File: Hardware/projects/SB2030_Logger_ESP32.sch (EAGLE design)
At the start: 34 parts, among them SW1 CKTACTSWITCH, U1 ESP-WROOM-32, U2 MCP2562, U3 NCP1117ST50T3G, U4 NCP1117ST33T3G, U5 SN65C1168PWR, X1 1751280

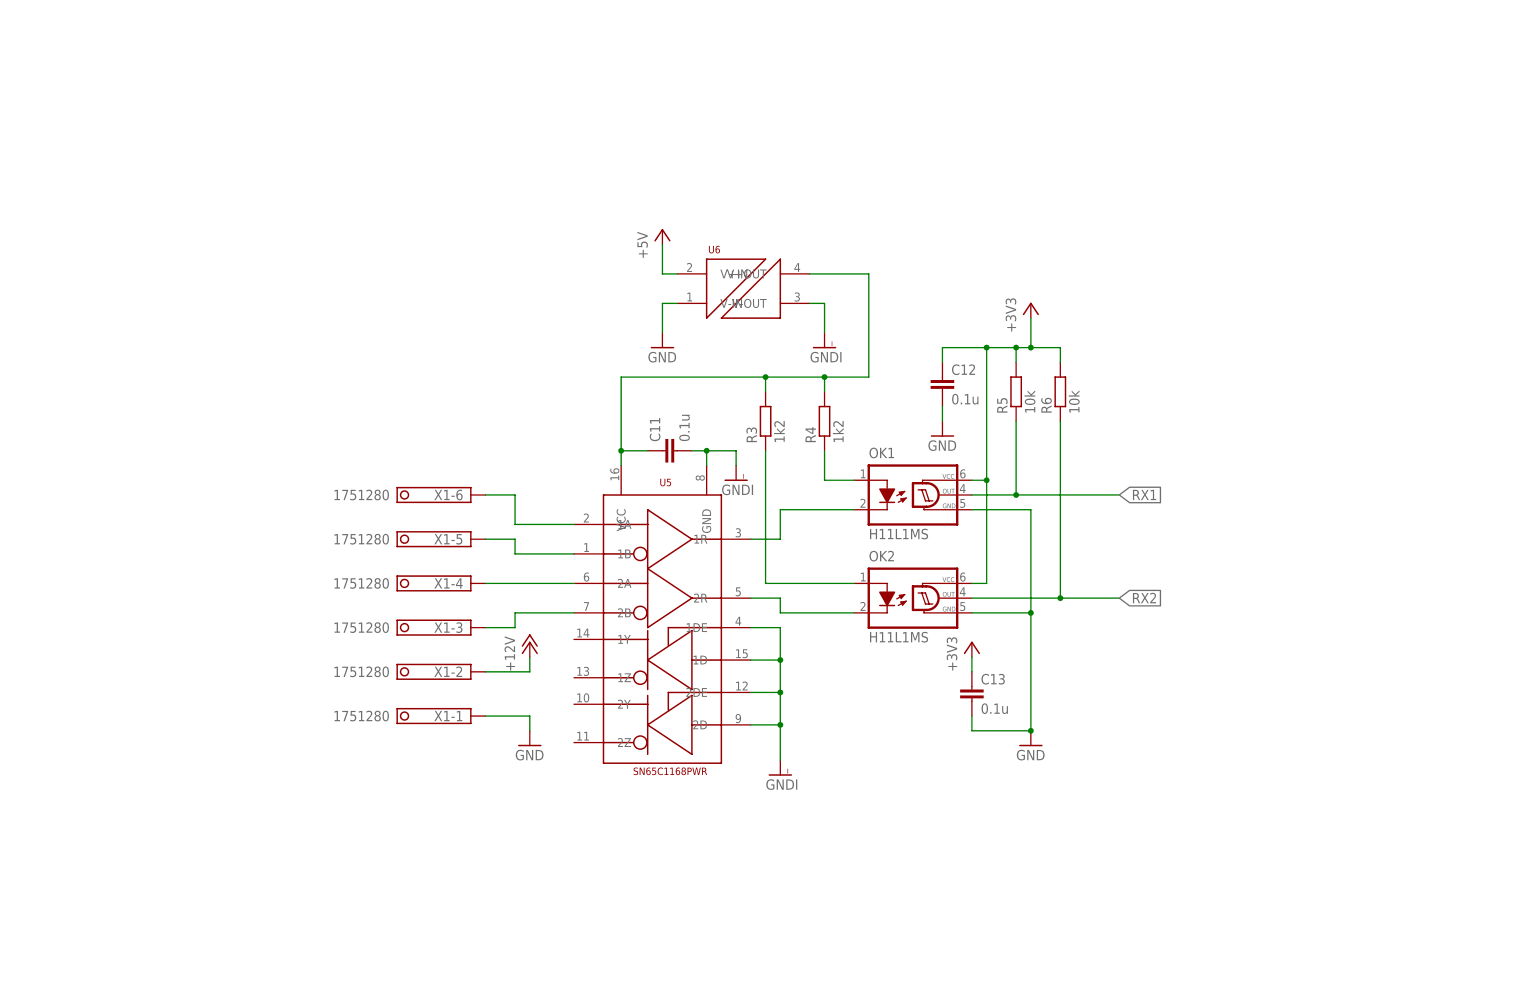
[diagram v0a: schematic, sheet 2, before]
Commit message: Major updates to SMD board design (added motion sensor and power management), with re-layout for production. Added Gerbers, BOM, and CPL for JLCPCB production. Added library for MPU6050 IMU. Added CCOM logo for silkscreen.
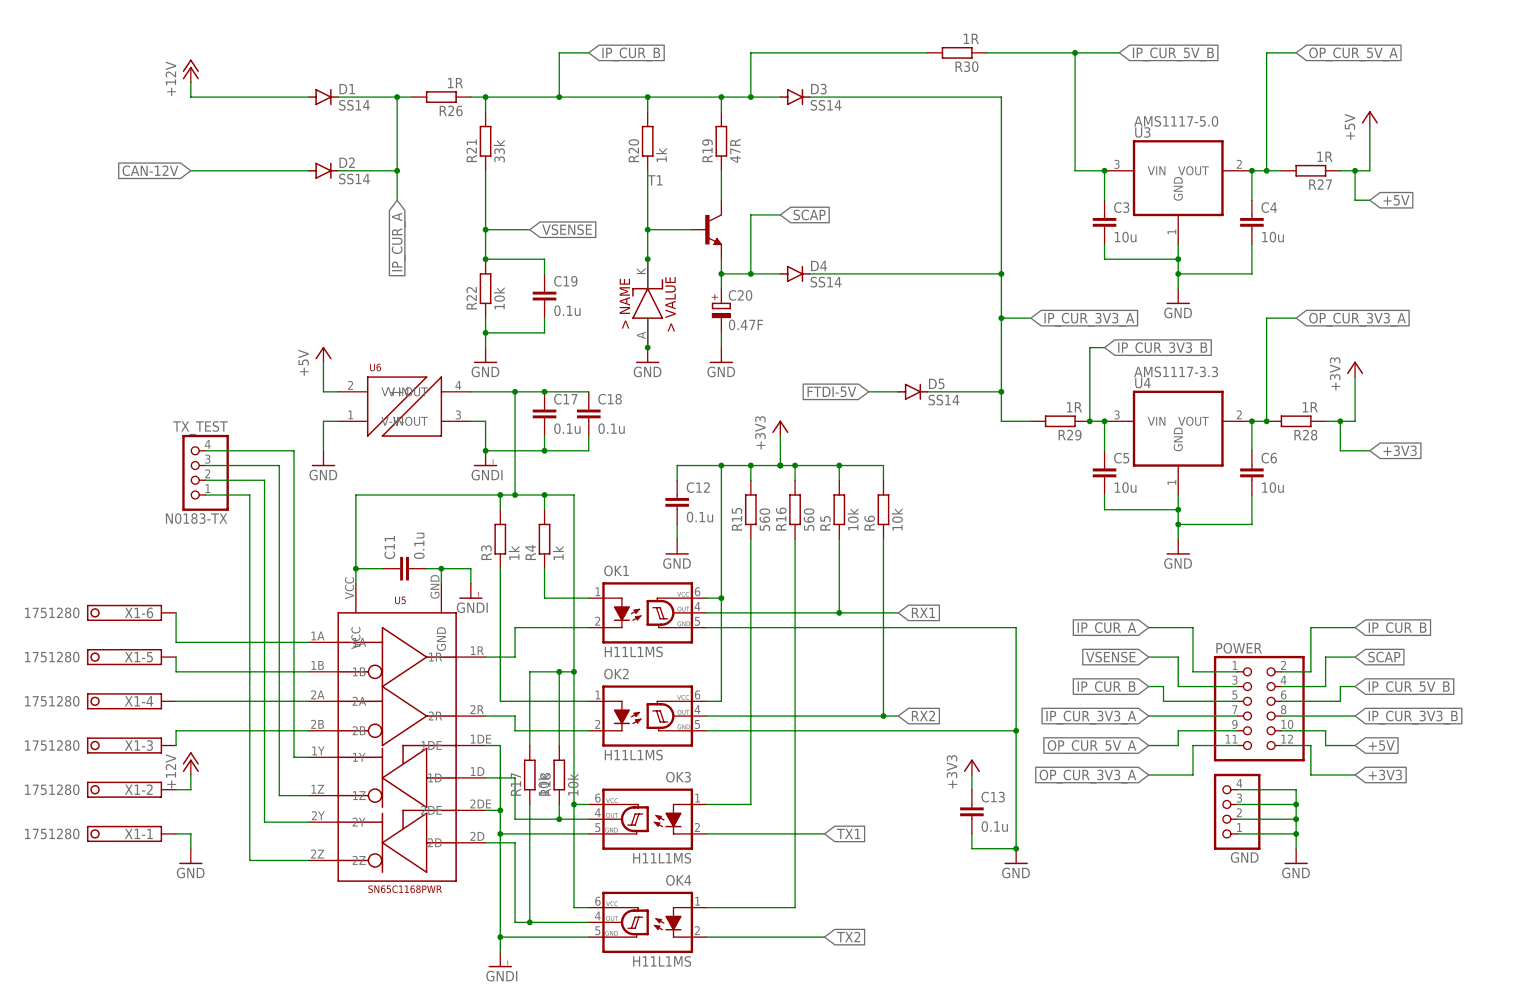
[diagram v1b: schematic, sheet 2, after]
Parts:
- removed JP1: FTDI/ICSP, pinhead:PINHD-1X6
- removed SDCARD: MicroSD Holder, 1140084168:1140084168
- removed SW1: CKTACTSWITCH, sb2030_logger:CKTACTSWITCH
- added C14: 2n2, rcl:C-EUC0805
- added C15, C17, C18, C19: 0.1u, rcl:C-EUC0805
- added C16: 10n, rcl:C-EUC0805
- added C20: 0.47F, rcl:CPOL-EUP128-50
- added CAN: CAN-TEST, pinhead:PINHD-1X2
- added D3, D4, D5: SS14, diode:CGRM4001-G
- added DZL4734: (no value), sb2030_logger:DZL4734
- added FTDI: FTDI/ICSP, pinhead:PINHD-1X6
- added GND: (no value), pinhead:PINHD-1X4
- added I2C: I2C_TEST, pinhead:PINHD-1X2
- added IC1: MPU6050, invensense:MPU6050
- added LED1, LED2, LED3: (no value), led:LEDCHIP-LED0603
- added N0183-TX: TX_TEST, pinhead:PINHD-1X4
- added NMEA2000: NMEA2000-2, pinhead:PINHD-1X4
- added OK3, OK4: H11L1MS, optocoupler:H11L1MS
- added POWER: (no value), pinhead:PINHD-2X6
- added PROG: PROG, pinhead:PINHD-1X2
- added R10, R11, R12, R13, R14, R9: 47k, rcl:R-EU_R0805
- added R15, R16: 560, rcl:R-EU_R0805
- added R17, R18, R22, R7, R8: 10k, rcl:R-EU_R0805
- added R19: 47R, rcl:R-EU_R0805
- added R20: 1k, rcl:R-EU_R0805
- added R21: 33k, rcl:R-EU_R0805
- added R23, R24, R25: 220, rcl:R-EU_R0805
- added R26, R27, R28, R29, R30: 1R, rcl:R-EU_R0805
- added R31: 6k8, rcl:R-EU_R0805
- added RESET: RESET, pinhead:PINHD-1X2
- added SDIO: SDIO_TEST, pinhead:PINHD-1X6
- added SJ1, SJ2, SJ3: (no value), jumper:SJ
- added T1: (no value), transistor:BC817-16-NPN-SOT23-BEC
- added T2, T3, T4: S8050, transistor:BC846
- added U$1: MICRO-SD, sb2030_logger:XUNPU-MICROSD-SOCKET
- D1, D2: value 1N5819 -> SS14; device sb2030_logger:1N5819HW-7-F -> diode:CGRM4001-G
- R3, R4: value 1k2 -> 1k
- U3: value NCP1117ST50T3G -> AMS1117-5.0
- U4: value NCP1117ST33T3G -> AMS1117-3.3
- U5: device sb2030_logger:SN65C1168PWR -> sb2030_logger:SN65C1168-SOIC
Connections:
- removed net VIN: C3.1, C5.1, D1.2, D2.2, U3.VIN, U4.VIN
- new net CAN-12V: D2.A, JP2.12V, NMEA2000.1
- new net FTDI-5V: D5.A, FTDI.3
- new net IP_CUR_3V3_A: D3.C, D4.C, D5.C, POWER.7, R29.2
- new net IP_CUR_3V3_B: C5.1, POWER.8, R29.1, U4.VIN
- new net IP_CUR_5V_B: C3.1, POWER.6, R30.1, U3.VIN
- new net IP_CUR_A: D1.C, D2.C, POWER.1, R26.2
- new net IP_CUR_B: D3.A, POWER.2, POWER.5, R19.2, R20.2, R21.2, R26.1, R30.2
- new net N$11: R10.1, SDIO.2, U$1.DAT1, U1.IO4
- new net N$23: C14.1, IC1G$1.CPOUT
- new net N$24: R12.1, SDIO.4, U$1.DAT3, U1.IO13
- new net N$25: R13.1, SDIO.5, U$1.CLK, U1.IO14
- new net N$26: R14.1, SDIO.6, U$1.CMD, U1.IO15
- new net N$27: N0183-TX.4, U5.1Y
- new net N$28: N0183-TX.3, U5.1Z
- new net N$29: N0183-TX.2, U5.2Y
- new net N$3: R1.1, SJ1.2
- new net N$30: N0183-TX.1, U5.2Z
- new net N$31: OK3.A, R15.1
- new net N$32: OK4.A, R16.1
- new net N$33: OK3.OUT, R18.1, U5.1D
- new net N$34: OK4.OUT, R17.1, U5.2D
- new net N$35: LED1.C, U1.IO25
- new net N$36: LED2.C, U1.IO26
- new net N$37: PROG.2, T2.B, T3.B, T4.B
- new net N$38: LED3.C, U1.IO27
- new net N$39: LED1.A, R23.2
- new net N$40: LED2.A, R24.2
- new net N$41: DZL4734.K, R20.1, T1.B
- new net N$42: R19.1, T1.C
- new net N$43: PROG.1, R31.1
- new net N$44: LED3.A, R25.2
- new net OP_CUR_3V3_A: C6.1, POWER.11, R28.2, U4.VOUT
- new net OP_CUR_5V_A: C4.1, POWER.9, R27.2, U3.VOUT
- new net SCAP: C20.+, D4.A, POWER.4, T1.E
- new net TX1: OK3.C, U1.IO18
- new net TX2: OK4.C, U1.IO19
- new net VSENSE: C19.1, POWER.3, R21.1, R22.2, U1.SENSOR_VP
- net +12V: now also D1.A; no longer D1.1
- net +3V3: now also C16.1, IC1G$1.VDD, IC1G$1.VLOGIC, POWER.12, R10.2, R11.2, R12.2, R13.2, R14.2, R15.2, R16.2, R23.1, R24.1, R25.1, R28.1, R31.2, R7.2, R8.2, R9.2, U$1.VCC; no longer C6.1, SDCARD.4, U4.VOUT
- net +5V: now also POWER.10, R27.1; no longer C4.1, U3.VOUT
- net GND: now also C14.2, C15.2, C16.2, C19.2, C20.-, DZL4734.A, FTDI.1, GND.1, GND.2, GND.3, GND.4, IC1G$1.AD0, IC1G$1.CLKIN, IC1G$1.FSYNC, IC1G$1.GND, IC1G$1.GND@1, NMEA2000.4, R22.1, RESET.2, T2.E, T3.E, T4.E, U$1.GND, U$1.GND1, U$1.GND2, U$1.GND3, U$1.GND4; no longer JP1.1, SDCARD.6, SW1.3, SW1.4
- net GNDI: now also C17.2, C18.2, OK3.GND, OK4.GND; no longer U5.1D, U5.2D
- net N$1: now also NMEA2000.2, R1.2; no longer R1.1
- net N$10: now also R11.1, SDIO.3, SJ3.1, SJ3.2, T4.C, U$1.DAT2, U1.IO12; no longer SDCARD.7, U1.IO19
- net N$12: now also T2.C; no longer SW1.1, SW1.2
- net N$2: now also NMEA2000.3, SJ1.1; no longer R1.2
- net N$21: now also C17.1, C18.1, OK3.VCC, OK4.VCC, R17.2, R18.2
- net N$22: now also R9.1, SDIO.1, SJ2.1, SJ2.2, T3.C, U$1.DAT0, U1.IO2; no longer D2.1, JP2.12V
- net N$4: now also RESET.1
- net N$5: now also I2C.2, IC1G$1.SCL, R7.1, U1.IO22; no longer SDCARD.2, U1.IO5
- net N$6: now also CAN.2
- net N$7: now also CAN.1, U1.IO17; no longer U1.IO4
- net N$8: now also I2C.1, IC1G$1.SDA, R8.1, U1.IO21; no longer SDCARD.3, U1.IO23
- net N$9: now also C15.1, IC1G$1.REGOUT; no longer SDCARD.5, U1.IO18
- net RX1: now also U1.IO34; no longer U1.IO13
- net RX2: now also U1.IO35; no longer U1.IO14
- net RXDATA: now also FTDI.5; no longer JP1.5
- net TXDATA: now also FTDI.4; no longer JP1.4
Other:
- moved on the sheet: C10, C11, C12, C13, C7, C8, C9, OK1, OK2, R1, R2, R3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

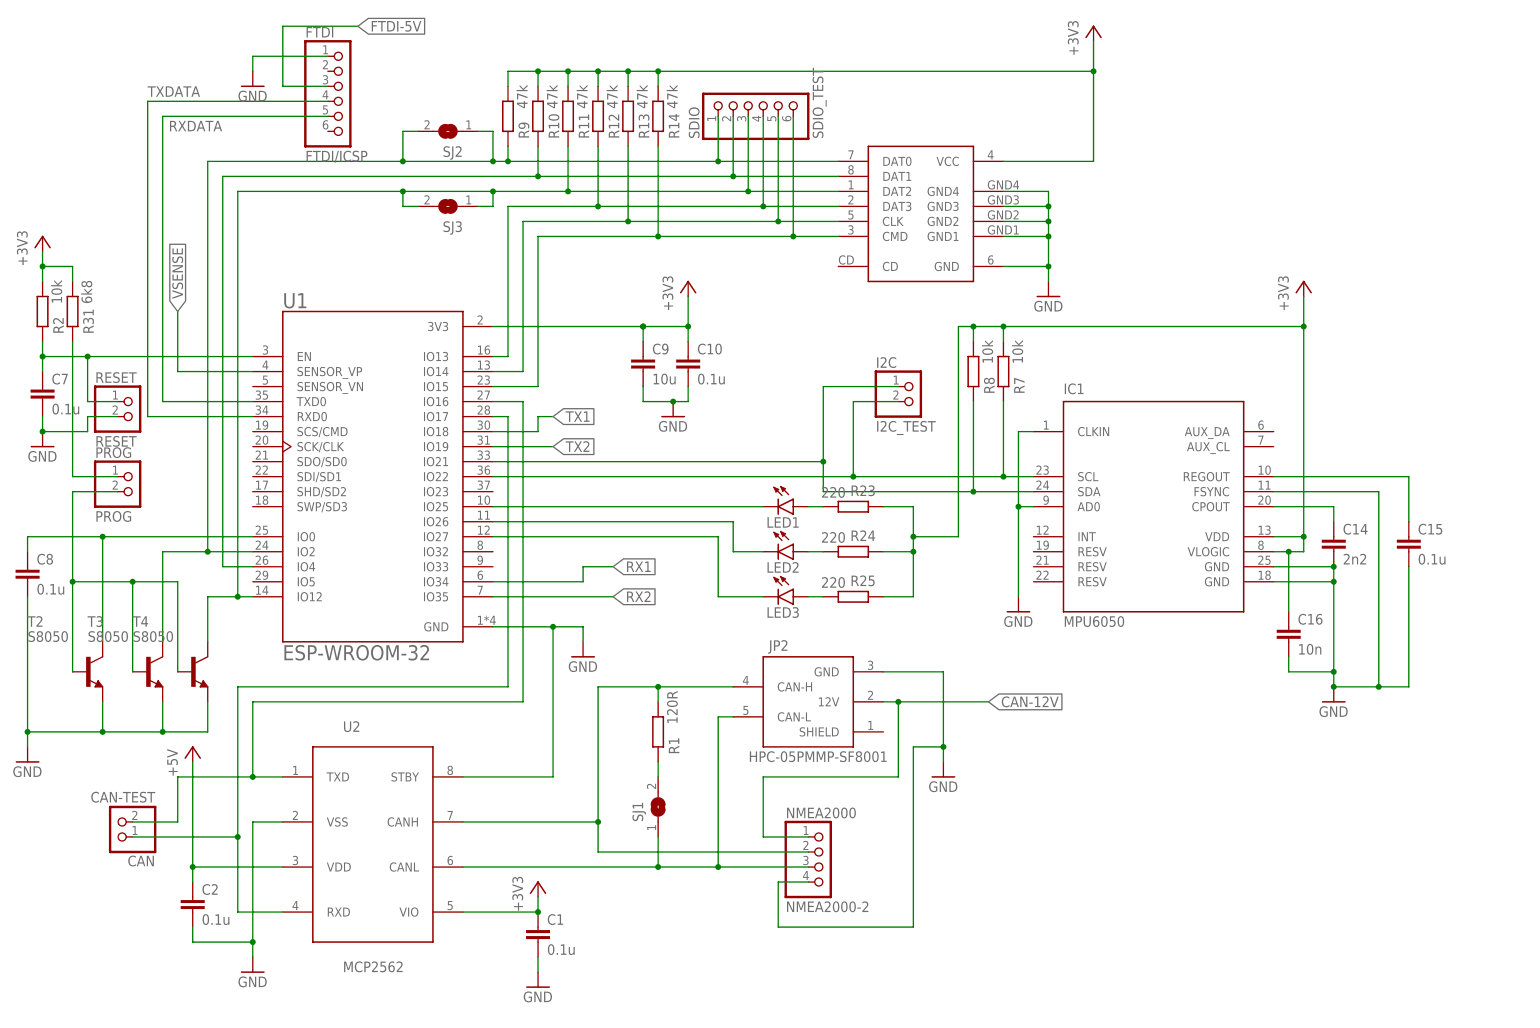
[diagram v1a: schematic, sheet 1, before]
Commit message: Updates to library specifications for devices, and schematic/board to match in order to give better match to actual components; V2.3 of demonstration board.
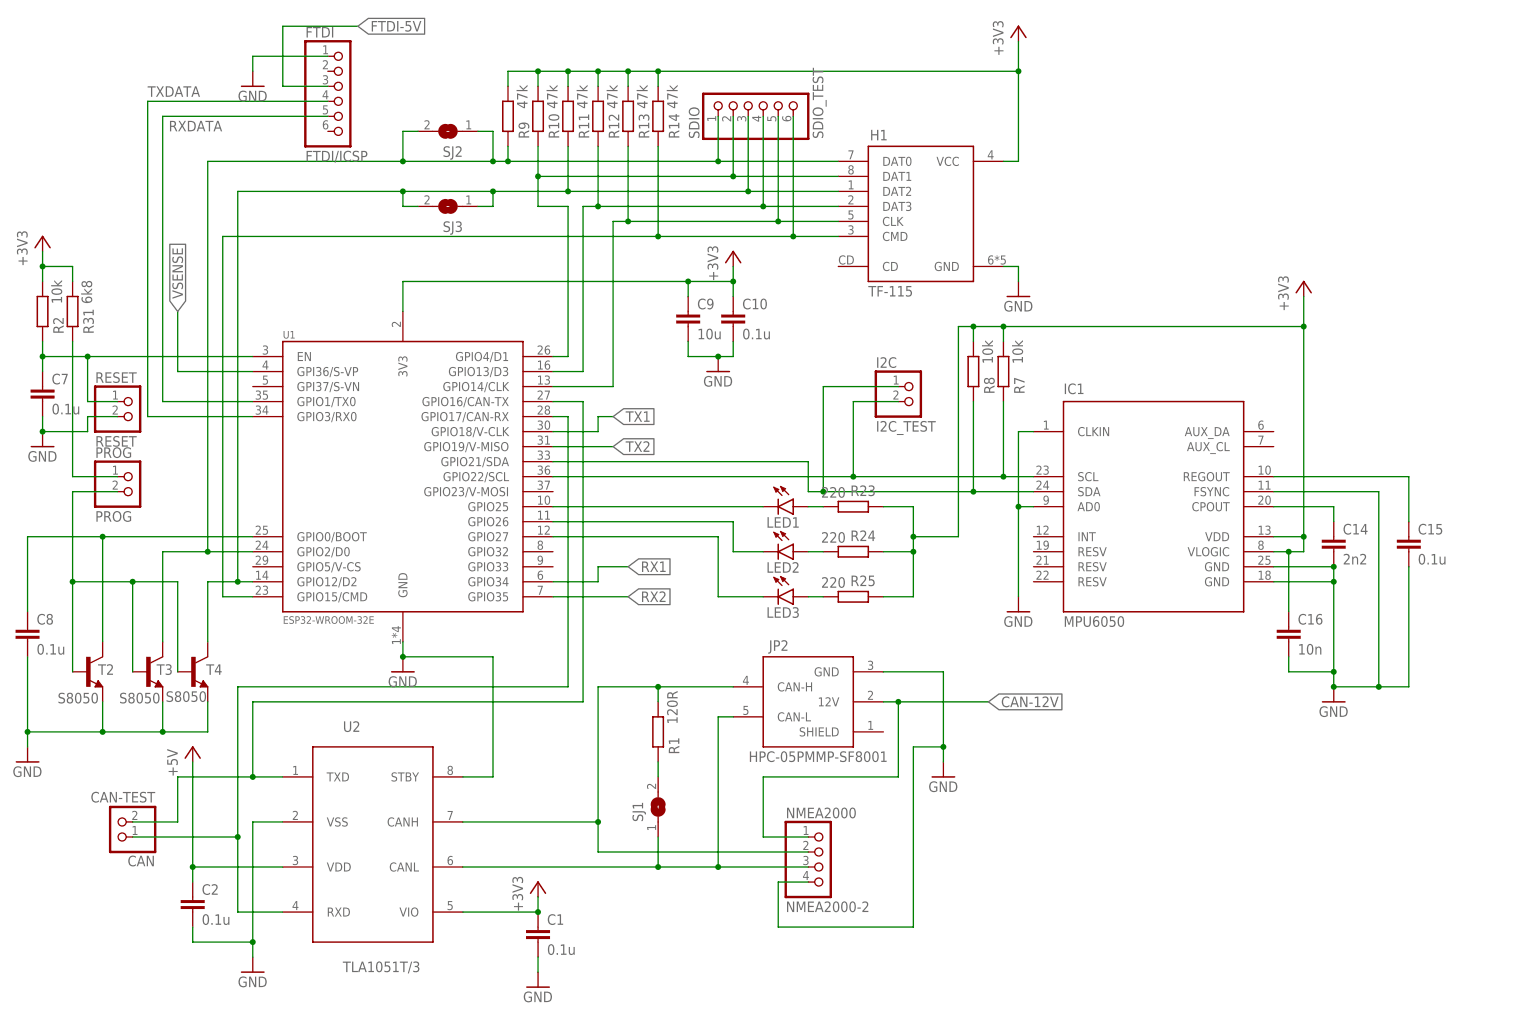
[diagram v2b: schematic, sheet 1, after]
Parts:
- removed DZL4734: (no value), sb2030_logger:DZL4734
- removed U$1: MICRO-SD, sb2030_logger:XUNPU-MICROSD-SOCKET
- added H1: TF-115, sb2030_logger:XUNPU-MICROSD-SOCKET
- added Z1: DZL4734, sb2030_logger:DZL4734
- D1, D2, D3, D4, D5: device diode:CGRM4001-G -> sb2030_logger:SS14
- U1: value ESP-WROOM-32 -> ESP32-WROOM-32E; device ESP-WROOM-32:ESP-WROOM-32 -> sb2030_logger:ESP32-WROOM-32E
- U2: value MCP2562 -> TLA1051T/3
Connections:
- net +3V3: now also H1.VCC; no longer U$1.VCC
- net GND: now also H1.GND, Z1.A; no longer DZL4734.A, U$1.GND, U$1.GND1, U$1.GND2, U$1.GND3, U$1.GND4
- net IP_CUR_3V3_A: now also D3.K, D4.K, D5.K; no longer D3.C, D4.C, D5.C
- net IP_CUR_A: now also D1.K, D2.K; no longer D1.C, D2.C
- net N$10: now also H1.DAT2, U1.GPIO12/D2; no longer U$1.DAT2, U1.IO12
- net N$11: now also H1.DAT1, U1.GPIO4/D1; no longer U$1.DAT1, U1.IO4
- net N$12: now also U1.GPIO0/BOOT; no longer U1.IO0
- net N$22: now also H1.DAT0, U1.GPIO2/D0; no longer U$1.DAT0, U1.IO2
- net N$24: now also H1.DAT3, U1.GPIO13/D3; no longer U$1.DAT3, U1.IO13
- net N$25: now also H1.CLK, U1.GPIO14/CLK; no longer U$1.CLK, U1.IO14
- net N$26: now also H1.CMD, U1.GPIO15/CMD; no longer U$1.CMD, U1.IO15
- net N$35: now also U1.GPIO25; no longer U1.IO25
- net N$36: now also U1.GPIO26; no longer U1.IO26
- net N$38: now also U1.GPIO27; no longer U1.IO27
- net N$41: now also Z1.K; no longer DZL4734.K
- net N$5: now also U1.GPIO22/SCL; no longer U1.IO22
- net N$6: now also U1.GPIO16/CAN-TX; no longer U1.IO16
- net N$7: now also U1.GPIO17/CAN-RX; no longer U1.IO17
- net N$8: now also U1.GPIO21/SDA; no longer U1.IO21
- net RX1: now also U1.GPIO34; no longer U1.IO34
- net RX2: now also U1.GPIO35; no longer U1.IO35
- net RXDATA: now also U1.GPIO1/TX0; no longer U1.TXD0
- net TX1: now also U1.GPIO18/V-CLK; no longer U1.IO18
- net TX2: now also U1.GPIO19/V-MISO; no longer U1.IO19
- net TXDATA: now also U1.GPIO3/RX0; no longer U1.RXD0
- net VSENSE: now also U1.GPI36/S-VP; no longer U1.SENSOR_VP
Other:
- moved on the sheet: C10, C8, C9

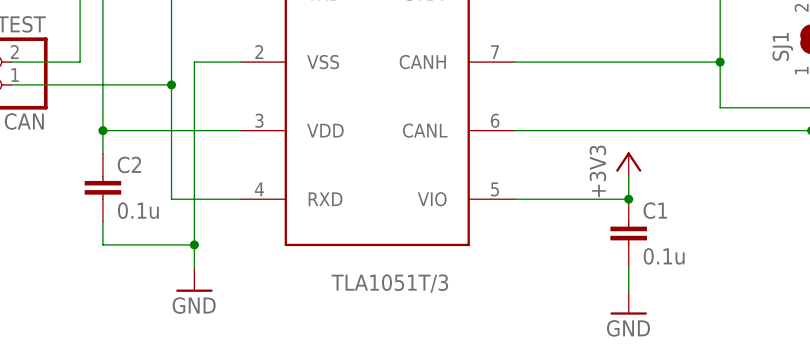
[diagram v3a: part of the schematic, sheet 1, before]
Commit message: Debugging fixes for NEMO-30 and WIBL support - Added builds for NEMO-30 separate from prototype loggers and WIBL - Added pass-back for value read from ADC for power monitoring - Pushed CAN traffic to GPIO16/17 to avoid interference with SD/MMC interface.
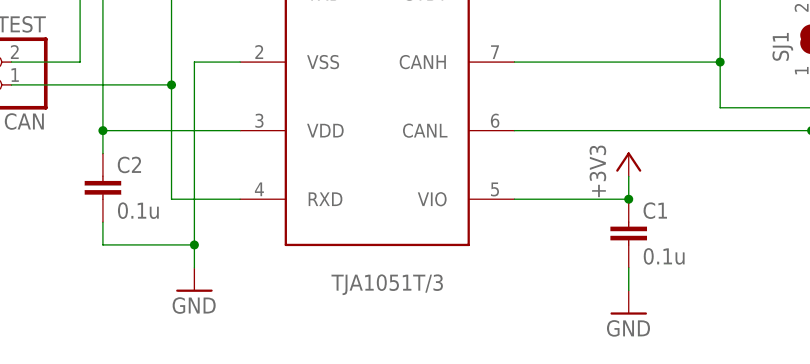
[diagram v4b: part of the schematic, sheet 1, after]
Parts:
- U2: value TLA1051T/3 -> TJA1051T/3
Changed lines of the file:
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@@
 <part name="C8" library="rcl" library_urn="urn:adsk.eagle:library:334" deviceset="C-EU" device="C0805" package3d_urn="urn:adsk.eagle:package:23617/2" value="0.1u"/>
 <part name="GND8" library="supply1" library_urn="urn:adsk.eagle:library:371" deviceset="GND" device=""/>
-<part name="U2" library="sb2030_logger" deviceset="MCP2562T-E/SN" device="" value="TLA1051T/3"/>
+<part name="U2" library="sb2030_logger" deviceset="MCP2562T-E/SN" device="" value="TJA1051T/3"/>
 <part name="GND9" library="supply1" library_urn="urn:adsk.eagle:library:371" deviceset="GND" device=""/>
 <part name="P+2" library="supply1" library_urn="urn:adsk.eagle:library:371" deviceset="+5V" device=""/>
